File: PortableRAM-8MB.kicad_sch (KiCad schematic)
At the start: 37 parts, among them J1 RAM Connector, J2 JTAG_Header_2.54mm_1x06, U1 ATF1502ASL, U11 74HC245, U12 74HC245, U2 AS6C8008-55TIN, U3 AS6C8008-55TIN, U4 AS6C8008-55TIN, U5 AS6C8008-55TIN, U6 AS6C8008-55TIN, U7 AS6C8008-55TIN, U8 AS6C8008-55TIN, U9 AS6C8008-55TIN

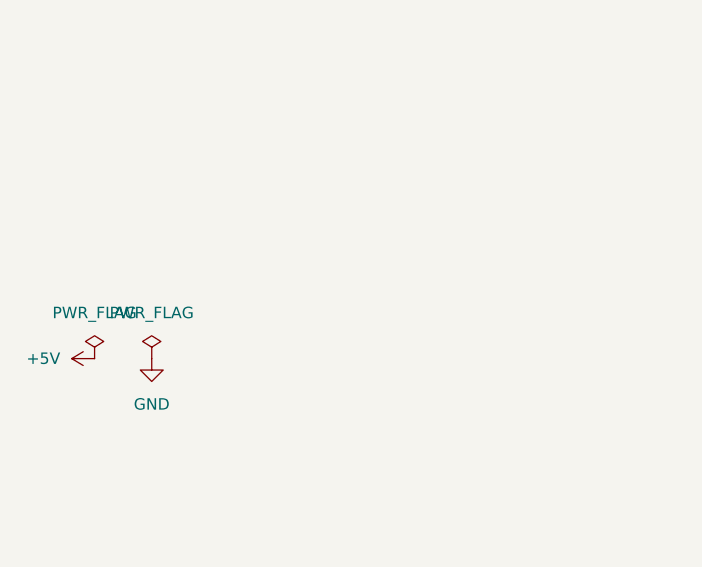
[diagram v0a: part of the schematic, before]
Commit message: Annotate the ERC power-anchor pair
Co-Authored-By: Claude Fable 5 <noreply@anthropic.com>
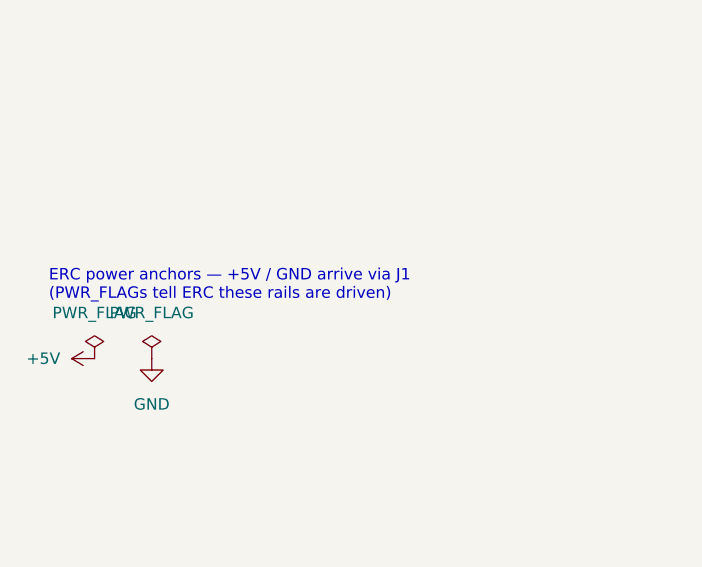
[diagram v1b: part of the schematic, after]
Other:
- note added: "ERC power anchors — +5V / GND arrive via J1 (PWR_FLAGs tell ERC these rails are driven)"
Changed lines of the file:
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@@
 		(comment 1 "Designed in North Carolina")
+	)
+	(text "ERC power anchors — +5V / GND arrive via J1\n(PWR_FLAGs tell ERC these rails are driven)"
+		(exclude_from_sim no)
+		(at 19.05 60.96 0)
+		(effects
+			(font
+				(size 1.27 1.27)
+			)
+			(justify left bottom)
+		)
 	)
 	(text "JTAG"
